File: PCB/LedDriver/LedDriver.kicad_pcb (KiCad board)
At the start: 2 copper layers, 125.7 x 125.7 mm, 189 parts, among them J101 LCD, J102 Conn_01x07_Female, J103 Conn_01x02_Male, J104 Conn_01x02_Male, J105 Conn_01x02_Male, J106 Conn_01x02_Male, J107 DC+5V, J108 Conn_01x08_Male, J109 Conn_01x08_Male, J110 Conn_01x08_Male, J111 Conn_01x02_Male, SW101 SW_Push, SW102 SW_Push, SW103 SW_Push, SW104 SW_Push, SW105 SW_Push, SW106 SW_Push, SW107 SW_Push, U101 MW-R-WX, U102 LM1117-3.3, U103 LM35-LP, U201 NJW4617DL3-TE1, U202 NJW4617DL3-TE1, U203 NJW4617DL3-TE1, U204 NJW4617DL3-TE1, U205 NJW4617DL3-TE1, U206 NJW4617DL3-TE1, U207 NJW4617DL3-TE1, U208 74HC595, U301 NJW4617DL3-TE1, U302 NJW4617DL3-TE1, U303 NJW4617DL3-TE1, U304 NJW4617DL3-TE1, U305 NJW4617DL3-TE1, U306 NJW4617DL3-TE1, U307 NJW4617DL3-TE1, U308 74HC595, U401 NJW4617DL3-TE1, U402 NJW4617DL3-TE1, U403 NJW4617DL3-TE1, U404 NJW4617DL3-TE1, U405 NJW4617DL3-TE1, U406 NJW4617DL3-TE1, U407 NJW4617DL3-TE1, U408 74HC595

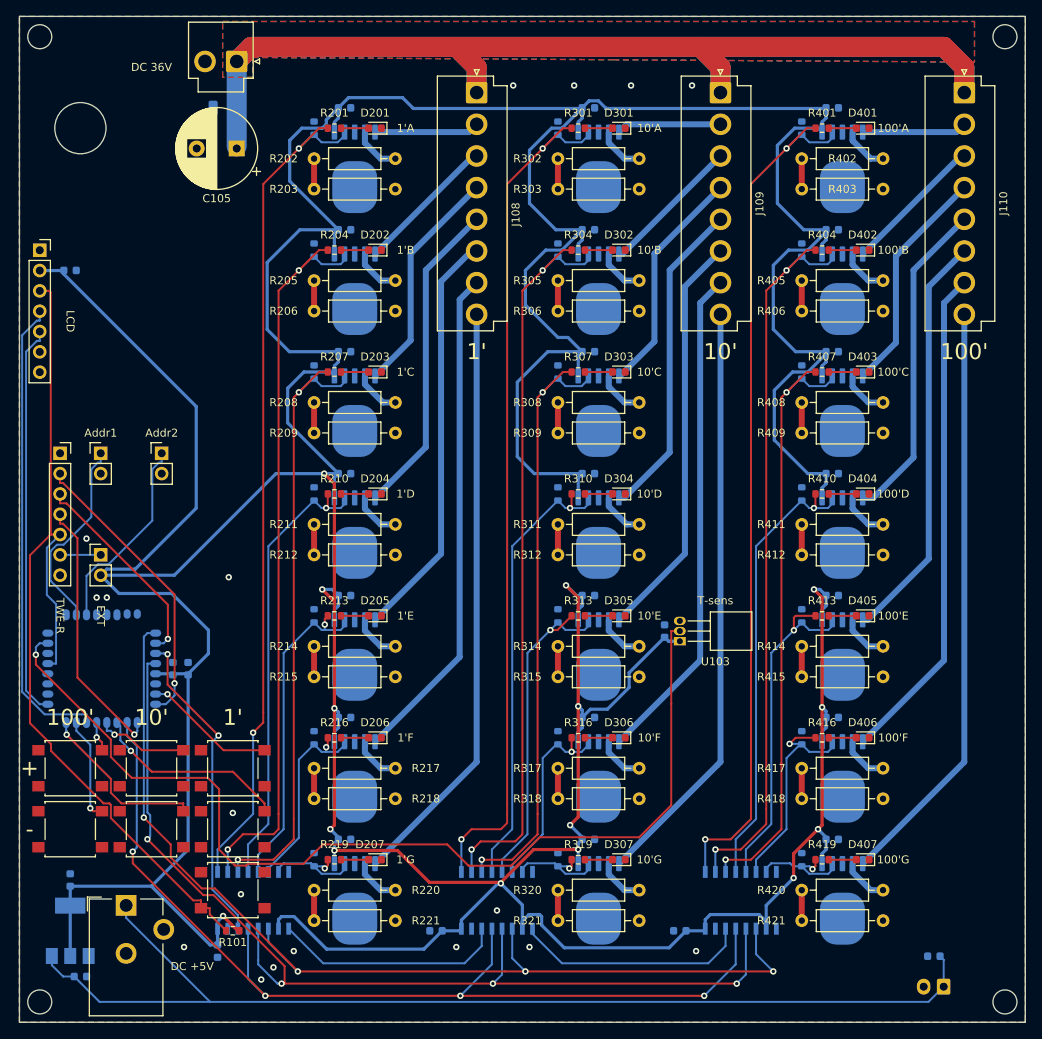
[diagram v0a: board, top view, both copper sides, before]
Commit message: シフトレジスタパターン移動
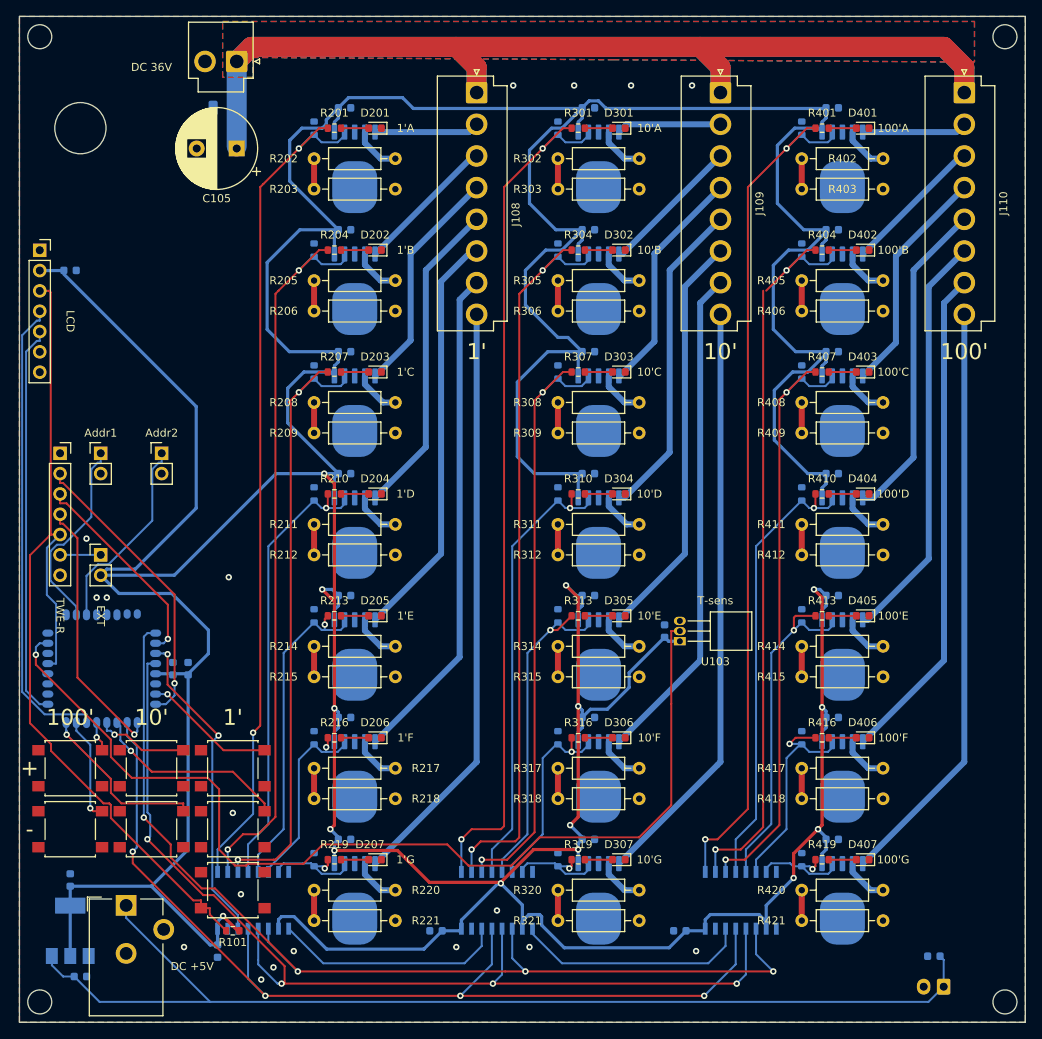
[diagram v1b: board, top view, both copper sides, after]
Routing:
- net /digitDriver_one/QB: track 93.6 -> 92.5 mm
- net /digitDriver_hun/QA: track 108.9 -> 108.0 mm

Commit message: スペーサ穴移動
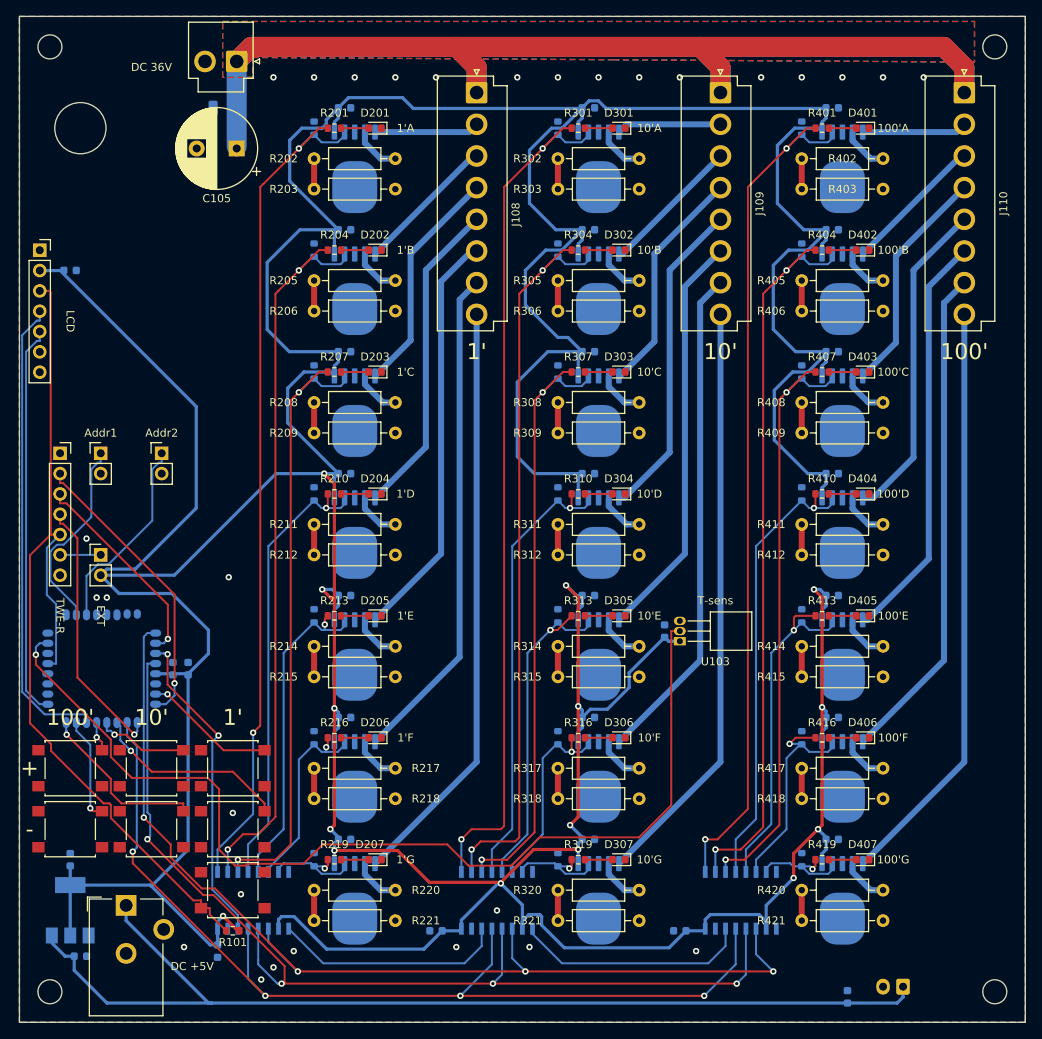
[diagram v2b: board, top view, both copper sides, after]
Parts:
- moved C108 11.9 mm to (224.2, 160.7), turned to 90 degrees
- moved J111 5.08 mm to (231.1, 159.4)
- moved U102 2.56 mm to (127.0, 149.8)
- moved C106 2.54 mm to (128.3, 155.6)
- moved C107 2.54 mm to (127.0, 143.5)
- moved H102 1.80 mm to (242.6, 41.9)
- moved H101 1.80 mm to (124.5, 41.9)
- moved H104 1.80 mm to (242.6, 160.0)
- moved H103 1.80 mm to (124.5, 160.0)
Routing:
- net Net-(C106-Pad1): track 135.7 -> 129.9 mm
- net GND: vias 18 -> 29

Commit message: 穴位置移動
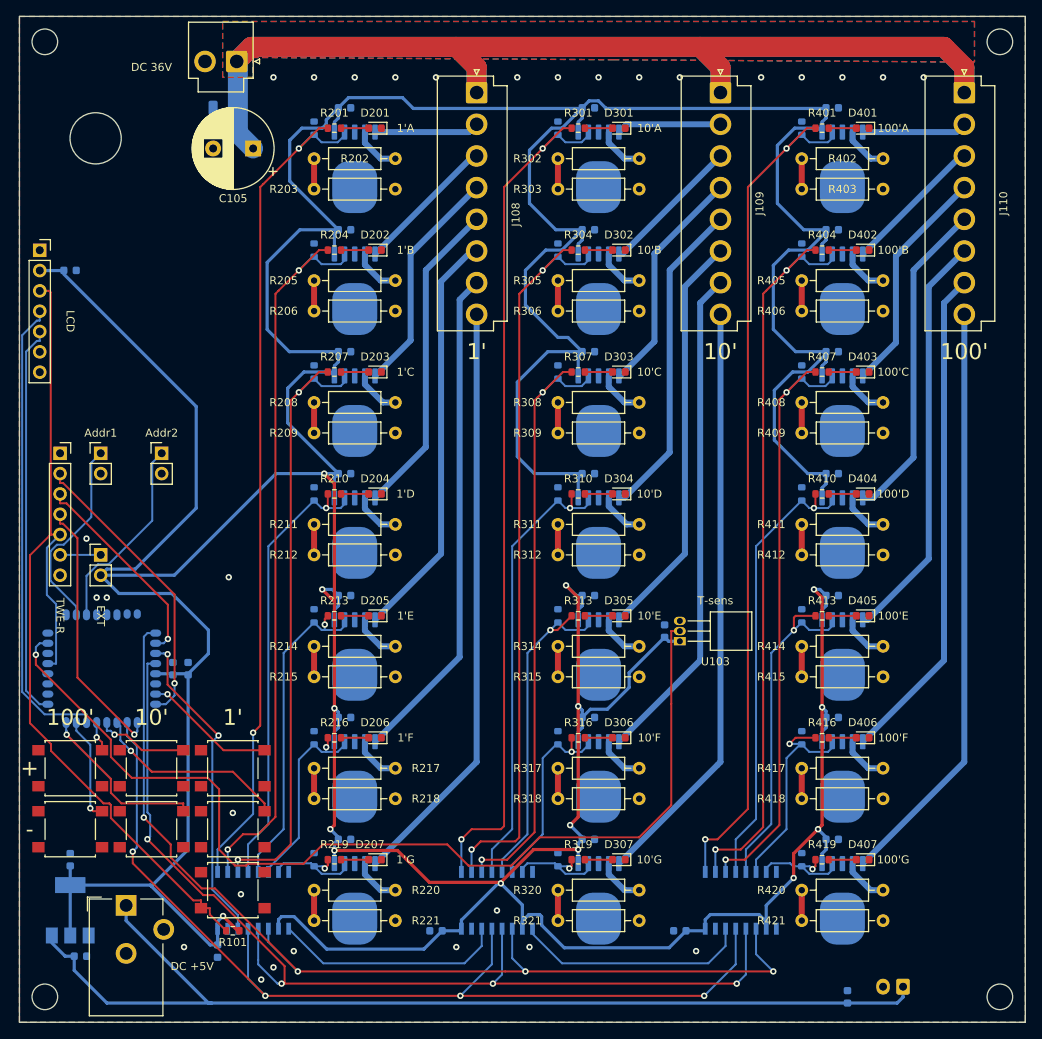
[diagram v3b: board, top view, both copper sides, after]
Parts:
- H101, H102, H103, H104: footprint MountingHole:MountingHole_3mm -> MountingHole:MountingHole_3.2mm_M3
- moved H105 2.29 mm to (130.2, 53.3)
- moved C105 2.05 mm to (149.9, 54.6)
- moved H102 0.90 mm to (243.2, 41.3)
- moved H104 0.90 mm to (243.2, 160.7)
- moved H101 0.90 mm to (123.8, 41.3)
- moved H103 0.90 mm to (123.8, 160.7)
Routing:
- net VDD: track 229.6 -> 230.7 mm
